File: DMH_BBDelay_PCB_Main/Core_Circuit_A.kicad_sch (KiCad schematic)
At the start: 82 parts, among them J22 Conn_01x04, J23 Conn_01x04, J24 Conn_01x04, J25 Conn_01x04, J26 Conn_01x08, J27 Conn_01x08, J28 Conn_01x08, J29 Conn_01x08, Q3 J113, SW3 SW_SPDT, U1 TL074, U2 TL074, U3 V3205, U4 CD4046, U9 40106

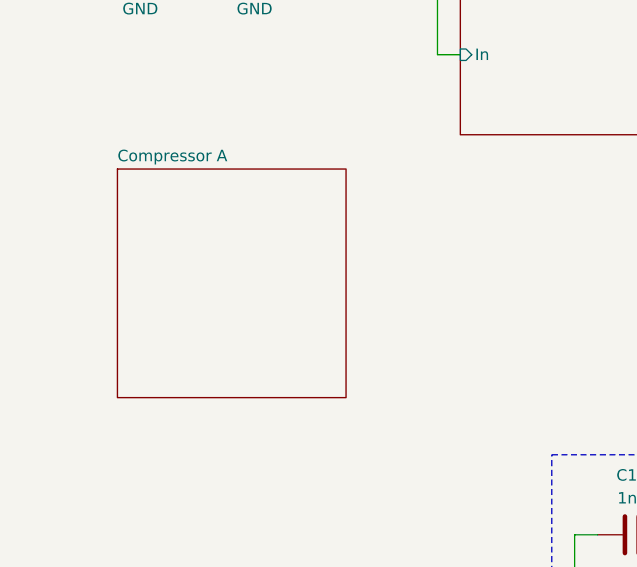
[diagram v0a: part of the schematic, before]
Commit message: Designed input compressor circuits
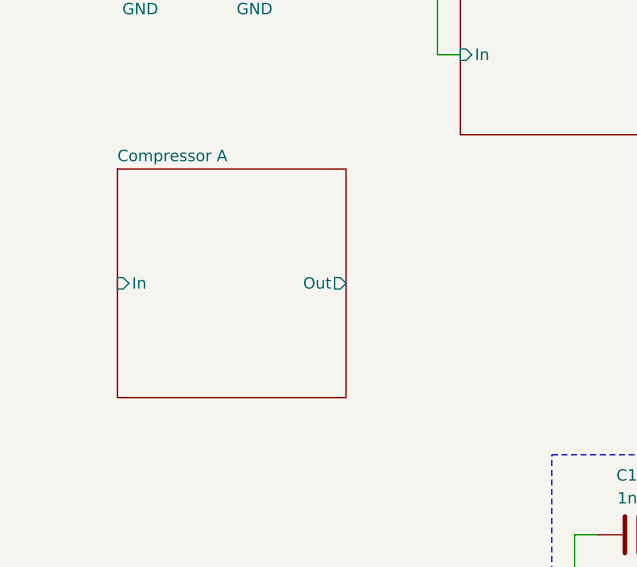
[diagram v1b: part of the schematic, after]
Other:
- sheet Compressor A ports: added In, Out; removed none
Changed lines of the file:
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@@
+			)
+		)
+		(pin "In" input
+			(at 25.4 114.3 180)
+			(effects
+				(font
+					(size 1.27 1.27)
+				)
+				(justify left)
+			)
+		)
+		(pin "Out" output
+			(at 50.8 114.3 0)
+			(effects
+				(font
+					(size 1.27 1.27)
+				)
+				(justify right)
 			)
 		)

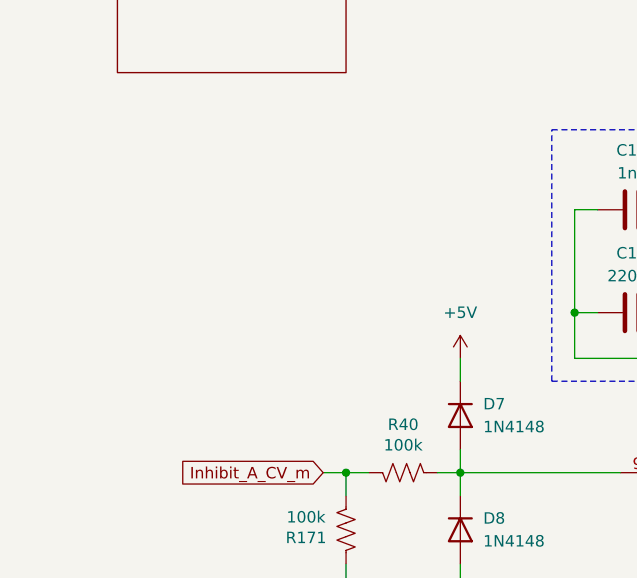
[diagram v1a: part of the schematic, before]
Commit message: Designed Expander circuits
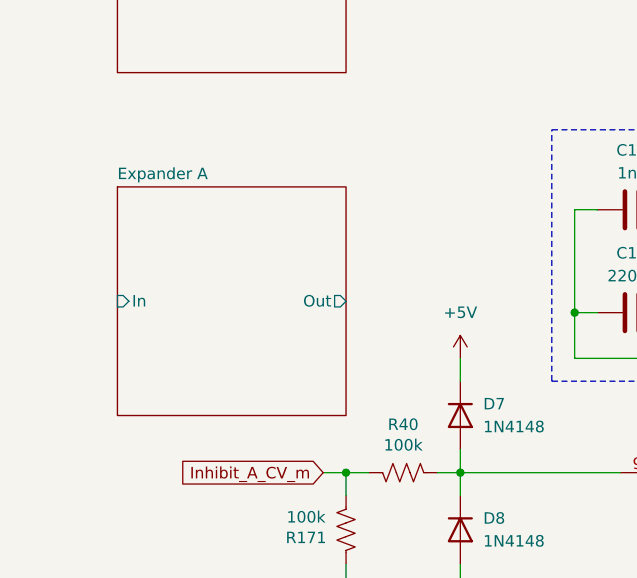
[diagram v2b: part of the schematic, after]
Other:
- added sheet Expander A (Expander_A.kicad_sch)
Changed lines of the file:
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@@
+	)
+	(sheet
+		(at 25.4 139.7)
+		(size 25.4 25.4)
+		(exclude_from_sim no)
+		(in_bom yes)
+		(on_board yes)
+		(dnp no)
+		(fields_autoplaced yes)
+		(stroke
+			(width 0.1524)
+			(type solid)
+		)
+		(fill
+			(color 0 0 0 0)
+		)
+		(property "Sheetname" "Expander A"
+			(at 25.4 138.9884 0)
+			(show_name no)
+			(do_not_autoplace no)
+			(effects
+				(font
+					(size 1.27 1.27)
+				)
+				(justify left bottom)
+			)
+		)
+		(property "Sheetfile" "Expander_A.kicad_sch"
+			(at 25.4 165.6846 0)
+			(hide yes)
+			(show_name no)
+			(do_not_autoplace no)
+			(effects
+				(font
+					(size 1.27 1.27)
+				)
+				(justify left top)
+			)
+		)
+		(pin "In" input
+			(at 25.4 152.4 180)
+			(effects
+				(font
+					(size 1.27 1.27)
+				)
+				(justify left)
+			)
+		)
+		(pin "Out" output
+			(at 50.8 152.4 0)
+			(effects
+				(font
+					(size 1.27 1.27)
+				)
+				(justify right)
+			)
+		)
+		(instances
+			(project "DMH_BBDelay_PCB_Main"
+				(path "/58f4306d-5387-4983-bb08-41a2313fd315/7ad2d702-dfb7-4d49-a82d-34430dd5948f"
+					(page "17")
+				)
+			)
+		)
 	)
 	(sheet

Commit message: Inserted compander in Channel A path
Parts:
- removed C18: 1uF Film, Capacitor_THT:C_Disc_D7.5mm_W5.0mm_P5.00mm, symbol Device:C
- removed C69: 100p, Capacitor_THT:C_Disc_D3.0mm_W2.0mm_P2.50mm, symbol Device:C
- removed C70, C73, C74: 1nF, Capacitor_THT:C_Disc_D4.3mm_W1.9mm_P5.00mm, symbol Device:C
- removed C71: 470pF, Capacitor_THT:C_Disc_D4.3mm_W1.9mm_P5.00mm, symbol Device:C
- removed C72: 220p, Capacitor_THT:C_Disc_D4.3mm_W1.9mm_P5.00mm, symbol Device:C
- removed R160: 47k, Resistor_THT:R_Axial_DIN0207_L6.3mm_D2.5mm_P7.62mm_Horizontal, symbol Device:R_US
- removed R187, R41: 120k, Resistor_THT:R_Axial_DIN0207_L6.3mm_D2.5mm_P7.62mm_Horizontal, symbol Device:R_US
- removed R188: 33k, Resistor_THT:R_Axial_DIN0207_L6.3mm_D2.5mm_P7.62mm_Horizontal, symbol Device:R_US
- removed R189, R190: 39k, Resistor_THT:R_Axial_DIN0207_L6.3mm_D2.5mm_P7.62mm_Horizontal, symbol Device:R_US
- removed R191: 43k, Resistor_THT:R_Axial_DIN0207_L6.3mm_D2.5mm_P7.62mm_Horizontal, symbol Device:R_US
- removed R42: 18k, Resistor_THT:R_Axial_DIN0207_L6.3mm_D2.5mm_P7.62mm_Horizontal, symbol Device:R_US
- removed unit 4 of U2
- R7: value 10k -> 100k
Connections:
- net Compressor A/In: now also R7.2, U1.7
- net Dry_A_Buff_m: now also R5.1
- net Input Filter A/Out: now also U3.7 (In); no longer R5.1
- net Output Filter A/In: now reaches U2.9 (-)
- net Output Filter A/In: now also U2.8
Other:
- added sheet Output Filter A (Output_filter_A.kicad_sch)
- note removed: "Used 124k"
- moved on the sheet: C42, C81, R1, R2, R5, R7, R84, R85, RV19, RV20, U1A, U1B

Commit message: Adjustments during breadboarding
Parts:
- added JP6: SolderJumper_2_Bridged, Jumper:SolderJumper-2_P1.3mm_Bridged_RoundedPad1.0x1.5mm, symbol Jumper:SolderJumper_2_Bridged
- added R243: 120k, Resistor_THT:R_Axial_DIN0207_L6.3mm_D2.5mm_P7.62mm_Horizontal, symbol Device:R_US
- added R244: 18k, Resistor_THT:R_Axial_DIN0207_L6.3mm_D2.5mm_P7.62mm_Horizontal, symbol Device:R_US
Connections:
- net GND: now also R244.1
- net Output Filter A/In: now also JP6.2 (B), R243.2; no longer U2.9 (-)
- new net: JP6.1 (A), R243.1, R244.2, U2.9 (-)

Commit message: Added notes from troubleshooting
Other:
- note added: "The feedback is entering runaway resonance at helf pot already. Try removing Tone Control from the feedback loop again to see if it improves. Note: the FB VCA will need to invert phase."
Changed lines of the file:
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@@
+		)
+	)
+	(text "The feedback is entering runaway resonance at helf pot already.\nTry removing Tone Control from the feedback loop again to see if it\nimproves. Note: the FB VCA will need to invert phase."
+		(exclude_from_sim no)
+		(at 371.602 118.11 0)
+		(effects
+			(font
+				(size 1.27 1.27)
+			)
 		)
 	)

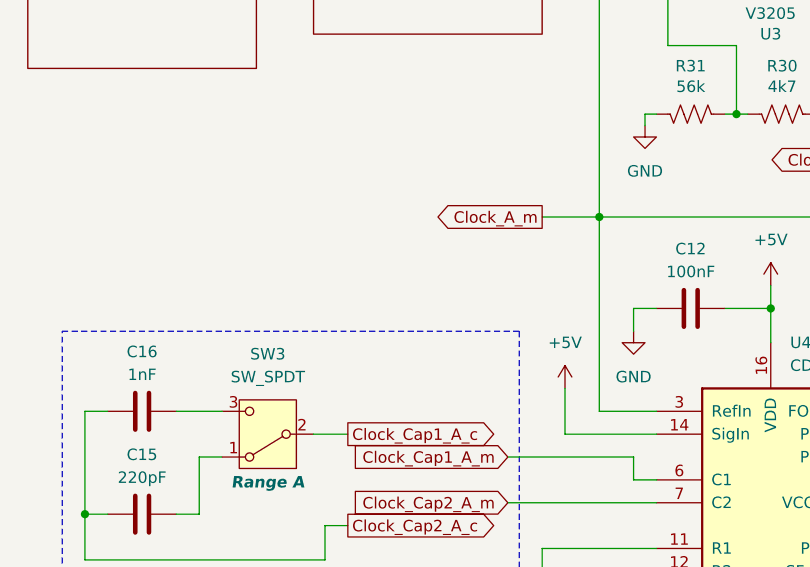
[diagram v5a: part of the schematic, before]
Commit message: Finished compander simulations
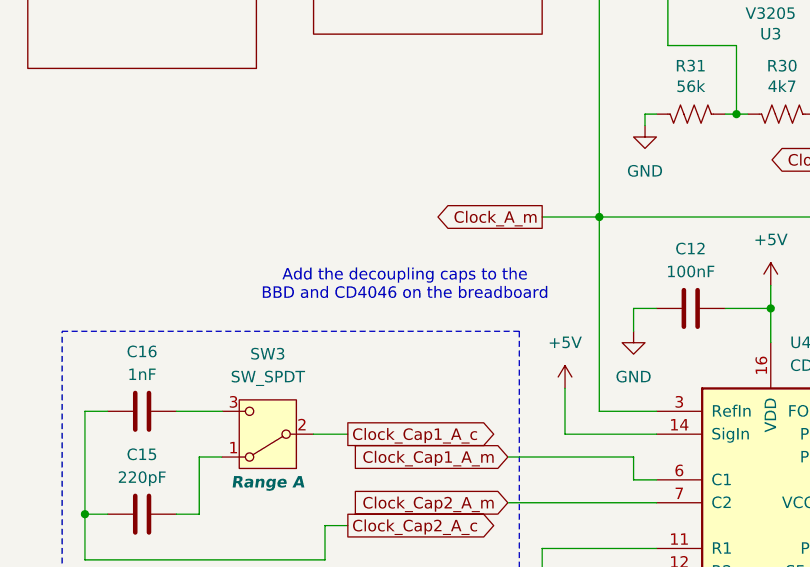
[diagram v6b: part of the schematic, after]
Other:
- note added: "Add the decoupling caps to the BBD and CD4046 on the breadboard"
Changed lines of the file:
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@@
+		)
+	)
+	(text "Add the decoupling caps to the\nBBD and CD4046 on the breadboard"
+		(exclude_from_sim no)
+		(at 111.76 128.27 0)
+		(effects
+			(font
+				(size 1.27 1.27)
+			)
 		)
 	)

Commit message: Tweaked compander
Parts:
- added C117: 33pF, Capacitor_THT:C_Disc_D3.0mm_W2.0mm_P2.50mm, symbol Device:C
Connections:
- net Compressor A/In: now also C117.2
- net at R5.2, R7.1, R8.1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: now also C117.1
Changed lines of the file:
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@@
 	)
 	(junction
-		(at 40.64 82.55)
+		(at 298.45 154.94)
 		(diameter 0)
 		(color 0 0 0 0)
 	)
 	(junction
-		(at 298.45 154.94)
+		(at 63.5 171.45)
 		(diameter 0)
 		(color 0 0 0 0)
 	)
 	(junction
-		(at 63.5 171.45)
+		(at 60.96 67.31)
 		(diameter 0)
 		(color 0 0 0 0)
@@
 	)
 	(junction
+		(at 60.96 82.55)
+		(diameter 0)
+		(color 0 0 0 0)
+	)
+	(junction
 		(at 177.8 69.85)
 		(diameter 0)
@@
 	)
 	(junction
+		(at 40.64 82.55)
+		(diameter 0)
+		(color 0 0 0 0)
+	)
+	(junction
 		(at 27.94 40.64)
 		(diameter 0)
@@
 	(wire
 		(pts
-			(xy 40.64 67.31) (xy 69.85 67.31)
+			(xy 40.64 67.31) (xy 60.96 67.31)
 		)
 		(stroke
@@
 	(wire
 		(pts
-			(xy 298.45 105.41) (xy 304.8 105.41)
+			(xy 60.96 67.31) (xy 60.96 71.12)
 		)
 		(stroke
@@
 	(wire
 		(pts
-			(xy 88.9 227.33) (xy 96.52 227.33)
+			(xy 298.45 105.41) (xy 304.8 105.41)
 		)
 		(stroke
@@
 	(wire
 		(pts
-			(xy 43.18 93.98) (xy 40.64 93.98)
+			(xy 88.9 227.33) (xy 96.52 227.33)
 		)
 		(stroke
@@
 	(wire
 		(pts
-			(xy 40.64 78.74) (xy 40.64 82.55)
+			(xy 43.18 93.98) (xy 40.64 93.98)
 		)
 		(stroke
@@
 	(wire
 		(pts
+			(xy 60.96 67.31) (xy 69.85 67.31)
+		)
+		(stroke
+			(width 0)
+			(type default)
+		)
+	)
+	(wire
+		(pts
 			(xy 209.55 31.75) (xy 278.13 31.75)
 		)
@@
 	(wire
 		(pts
+			(xy 60.96 78.74) (xy 60.96 82.55)
+		)
+		(stroke
+			(width 0)
+			(type default)
+		)
+	)
+	(wire
+		(pts
 			(xy 38.1 88.9) (xy 40.64 88.9)
 		)
@@
 	(wire
 		(pts
+			(xy 69.85 54.61) (xy 69.85 67.31)
+		)
+		(stroke
+			(width 0)
+			(type default)
+		)
+	)
+	(wire
+		(pts
 			(xy 267.97 149.86) (xy 267.97 157.48)
 		)
@@
 	(wire
 		(pts
-			(xy 40.64 67.31) (xy 40.64 71.12)
+			(xy 40.64 67.31) (xy 40.64 82.55)
 		)
 		(stroke
@@
 	(wire
 		(pts
-			(xy 69.85 31.75) (xy 69.85 67.31)
+			(xy 69.85 31.75) (xy 69.85 46.99)
 		)
 		(stroke
@@
 	)
 	(symbol
-		(lib_id "Device:R_US")
-		(at 40.64 74.93 0)
-		(mirror x)
-		(unit 1)
-		(body_style 1)
-		(exclude_from_sim no)
-		(in_bom yes)
-		(on_board yes)
-		(in_pos_files yes)
-		(dnp no)
-		(property "Reference" "R8"
-			(at 38.1 73.6599 0)
-			(show_name no)
-			(do_not_autoplace no)
-			(effects
-				(font
-					(size 1.27 1.27)
-				)
-				(justify right)
-			)
-		)
-		(property "Value" "100k"
-			(at 38.1 76.1999 0)
-			(show_name no)
-			(do_not_autoplace no)
-			(effects
-				(font
-					(size 1.27 1.27)
-				)
-				(justify right)
-			)
-		)
-		(property "Footprint" "Resistor_THT:R_Axial_DIN0207_L6.3mm_D2.5mm_P7.62mm_Horizontal"
-			(at 41.656 74.676 90)
-			(hide yes)
-			(show_name no)
-			(do_not_autoplace no)
-			(effects
-				(font
-					(size 1.27 1.27)
-				)
-			)
-		)
-		(property "Datasheet" ""
-			(at 40.64 74.93 0)
-			(hide yes)
-			(show_name no)
-			(do_not_autoplace no)
-			(effects
-				(font
-					(size 1.27 1.27)
-				)
-			)
-		)
-		(property "Description" "Resistor, US symbol"
-			(at 40.64 74.93 0)
-			(hide yes)
-			(show_name no)
-			(do_not_autoplace no)
-			(effects
-				(font
-					(size 1.27 1.27)
-				)
-			)
-		)
-		(pin "2"
-		)
-		(pin "1"
-		)
-		(instances
-			(project "DMH_BBDelay_PCB_Main"
-				(path "/58f4306d-5387-4983-bb08-41a2313fd315/7ad2d702-dfb7-4d49-a82d-34430dd5948f"
-					(reference "R8")
-					(unit 1)
-				)
-			)
-		)
-	)
-	(symbol
 		(lib_id "power:+5V")
 		(at 140.97 78.74 0)
@@
 	)
 	(symbol
+		(lib_id "Device:R_US")
+		(at 69.85 50.8 0)
+		(mirror x)
+		(unit 1)
+		(body_style 1)
+		(exclude_from_sim no)
+		(in_bom yes)
+		(on_board yes)
+		(in_pos_files yes)
+		(dnp no)
+		(property "Reference" "R8"
+			(at 67.31 49.5299 0)
+			(show_name no)
+			(do_not_autoplace no)
+			(effects
+				(font
+					(size 1.27 1.27)
+				)
+				(justify right)
+			)
+		)
+		(property "Value" "100k"
+			(at 67.31 52.0699 0)
+			(show_name no)
+			(do_not_autoplace no)
+			(effects
+				(font
+					(size 1.27 1.27)
+				)
+				(justify right)
+			)
+		)
+		(property "Footprint" "Resistor_THT:R_Axial_DIN0207_L6.3mm_D2.5mm_P7.62mm_Horizontal"
+			(at 70.866 50.546 90)
+			(hide yes)
+			(show_name no)
+			(do_not_autoplace no)
+			(effects
+				(font
+					(size 1.27 1.27)
+				)
+			)
+		)
+		(property "Datasheet" ""
+			(at 69.85 50.8 0)
+			(hide yes)
+			(show_name no)
+			(do_not_autoplace no)
+			(effects
+				(font
+					(size 1.27 1.27)
+				)
+			)
+		)
+		(property "Description" "Resistor, US symbol"
+			(at 69.85 50.8 0)
+			(hide yes)
+			(show_name no)
+			(do_not_autoplace no)
+			(effects
+				(font
+					(size 1.27 1.27)
+				)
+			)
+		)
+		(pin "2"
+		)
+		(pin "1"
+		)
+		(instances
+			(project "DMH_BBDelay_PCB_Main"
+				(path "/58f4306d-5387-4983-bb08-41a2313fd315/7ad2d702-dfb7-4d49-a82d-34430dd5948f"
+					(reference "R8")
+					(unit 1)
+				)
+			)
+		)
+	)
+	(symbol
 		(lib_id "Switch:SW_SPDT")
 		(at 96.52 144.78 180)
@@
 					(unit 1)
 				)
+			)
+		)
+	)
+	(symbol
+		(lib_id "Device:C")
+		(at 60.96 74.93 0)
+		(unit 1)
+		(body_style 1)
+		(exclude_from_sim no)
+		(in_bom yes)
+		(on_board yes)
+		(in_pos_files yes)
+		(dnp no)
+		(property "Reference" "C117"
+			(at 66.04 76.454 0)
+			(show_name no)
+			(do_not_autoplace no)
+			(effects
+				(font
+					(size 1.27 1.27)
+				)
+			)
+		)
+		(property "Value" "33pF"
+			(at 66.04 73.914 0)
+			(show_name no)
+			(do_not_autoplace no)
+			(effects
+				(font
+					(size 1.27 1.27)
+				)
+			)
+		)
+		(property "Footprint" "Capacitor_THT:C_Disc_D3.0mm_W2.0mm_P2.50mm"
+			(at 61.9252 78.74 0)
+			(hide yes)
+			(show_name no)
+			(do_not_autoplace no)
+			(effects
+				(font
+					(size 1.27 1.27)
+				)
+			)
+		)
+		(property "Datasheet" ""
+			(at 60.96 74.93 0)
+			(hide yes)
+			(show_name no)
+			(do_not_autoplace no)
+			(effects
+				(font
+					(size 1.27 1.27)
+				)
+			)
+		)
+		(property "Description" "Unpolarized capacitor"
+			(at 60.96 74.93 0)
+			(hide yes)
+			(show_name no)
+			(do_not_autoplace no)
+			(effects
+				(font
+					(size 1.27 1.27)
+				)
+			)
+		)
+		(property "Function" ""
+			(at 60.96 74.93 0)
+			(show_name no)
+			(do_not_autoplace no)
+			(effects
+				(font
+					(size 1.27 1.27)
+				)
+			)
+		)
+		(pin "1"
+		)
+		(pin "2"
+		)
+		(instances
+			(project "DMH_BBDelay_PCB_Main"
+				(path "/58f4306d-5387-4983-bb08-41a2313fd315/7ad2d702-dfb7-4d49-a82d-34430dd5948f"
+					(reference "C117")
+					(unit 1)
+				)

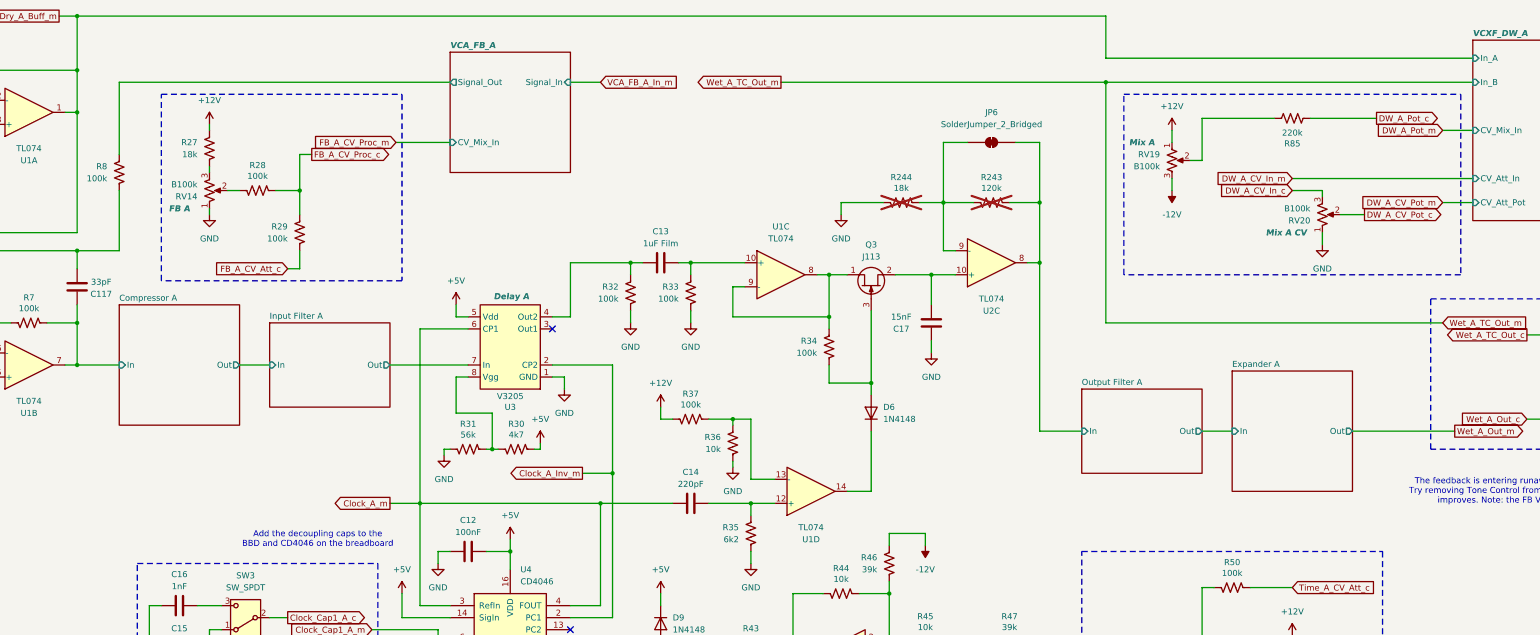
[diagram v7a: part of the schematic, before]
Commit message: Scaled up components in Tone Control part
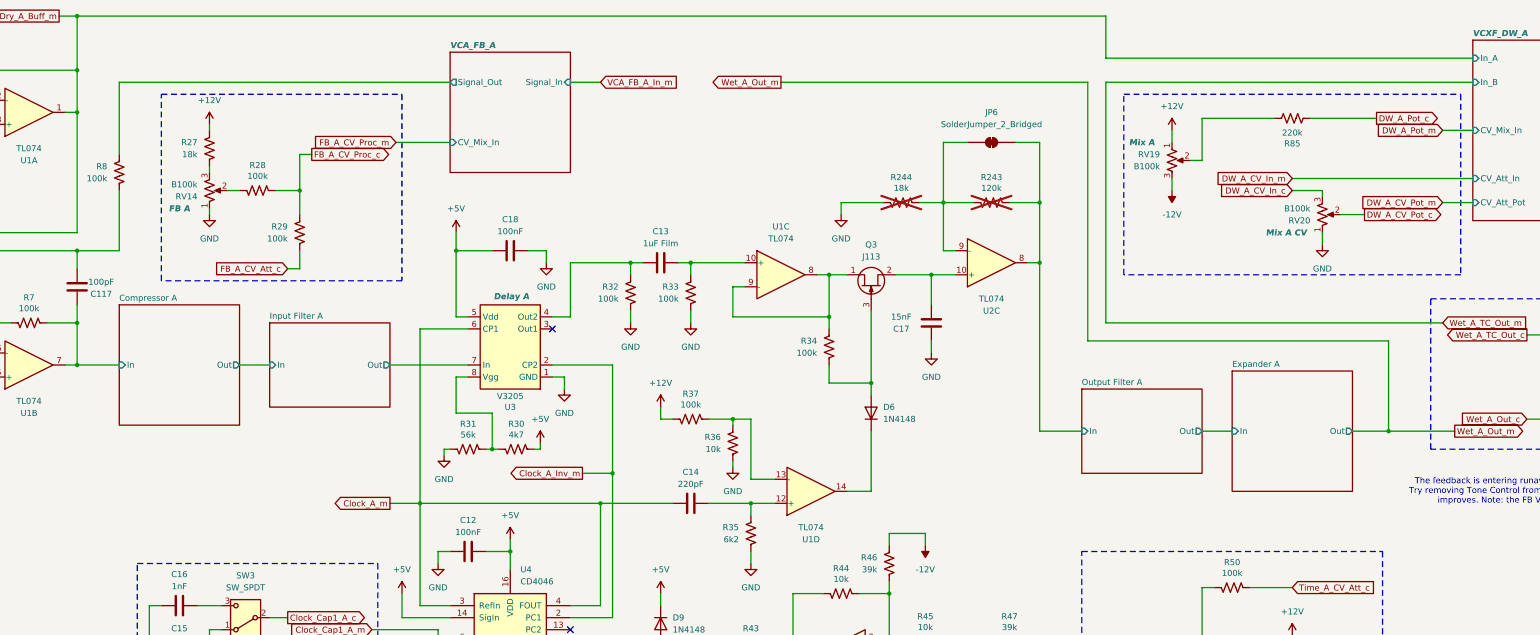
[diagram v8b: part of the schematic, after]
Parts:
- added C18: 100nF, Capacitor_THT:C_Disc_D4.3mm_W1.9mm_P5.00mm, symbol Device:C
- C117: value 33pF -> 100pF
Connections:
- net +5V: now also C18.1
- net GND: now also C18.2
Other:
- note removed: "Add the decoupling caps to the BBD and CD4046 on the breadboard"
